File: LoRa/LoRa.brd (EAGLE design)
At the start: 59.4 x 27.9 mm, 35 parts, among them J1 UP2-AH-1-TH, U1 STM32L053C8T6, U2 RFM69HCW, U5 LM3671MF-3.3/NOPB, X1 uFL/SMA, Y1 ECS-80-S-4X

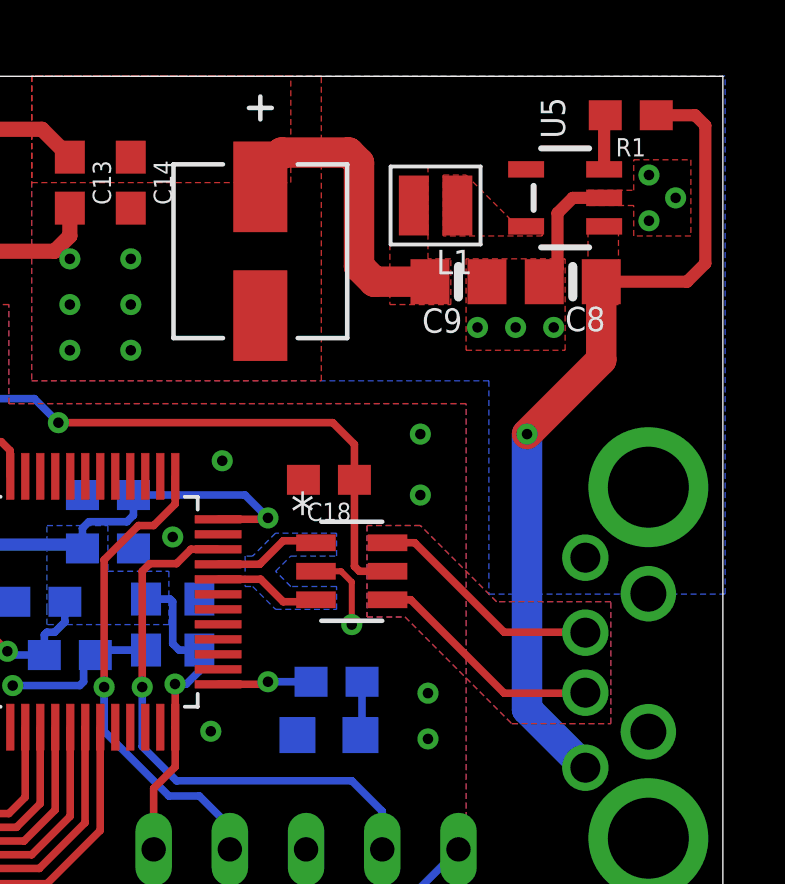
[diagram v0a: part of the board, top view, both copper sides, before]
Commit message: mounting hole and feedback trace
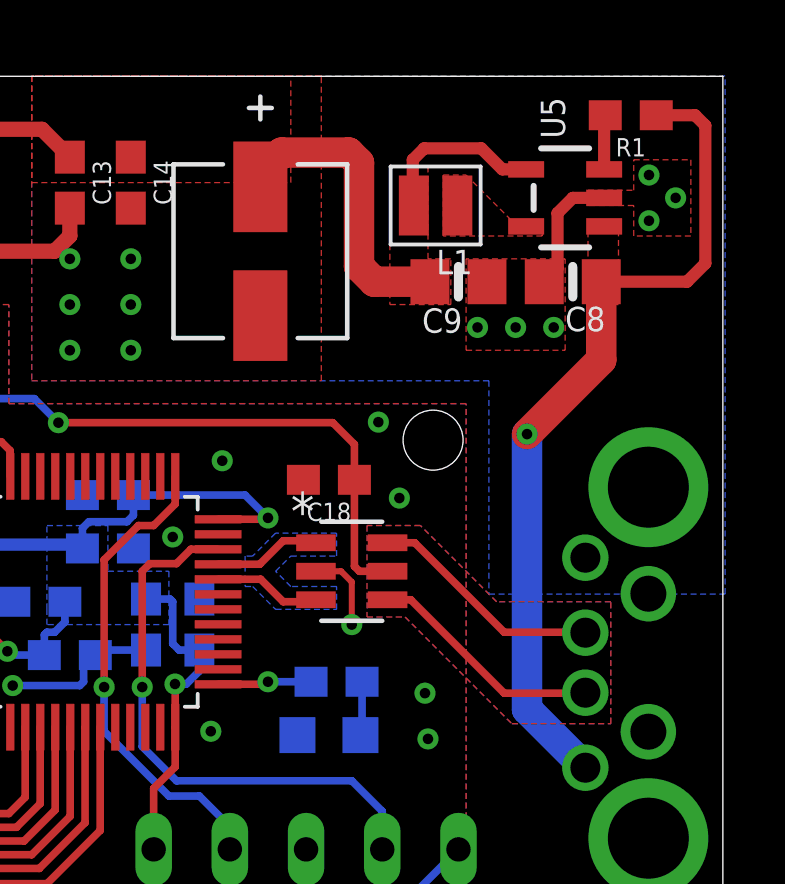
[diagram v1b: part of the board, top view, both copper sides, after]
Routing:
- net 3.3V: track 145.1 -> 150.9 mm
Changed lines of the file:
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@@
 <setting verticaltext="up"/>
 </settings>
-<grid distance="5" unitdist="mil" unit="mil" style="lines" multiple="1" display="yes" altdistance="5" altunitdist="mil" altunit="mil"/>
+<grid distance="0.1" unitdist="mm" unit="mm" style="lines" multiple="1" display="yes" altdistance="5" altunitdist="mil" altunit="mil"/>
 <layers>
 <layer number="1" name="Top" color="4" fill="1" visible="yes" active="yes"/>
@@
 <hole x="21" y="24.6" drill="2"/>
 <hole x="21" y="5.6" drill="2"/>
+<hole x="49.7" y="15.8" drill="2"/>
 </plain>
 <attributes>
@@
 <vertex x="36.322" y="27.94"/>
 </polygon>
-<via x="49.276" y="16.002" extent="1-16" drill="0.35"/>
-<via x="49.276" y="13.97" extent="1-16" drill="0.35"/>
+<via x="47.876" y="16.402" extent="1-16" drill="0.35"/>
+<via x="48.576" y="13.87" extent="1-16" drill="0.35"/>
 <wire x1="45.7962" y1="11.43" x2="46.6333375" y2="11.43" width="0.2032" layer="1"/>
 <wire x1="46.99" y1="11.0733375" x2="46.99" y2="9.652" width="0.2032" layer="1"/>
@@
 <via x="3.048" y="16.002" extent="1-16" drill="0.35"/>
 <via x="37.592" y="20.32" extent="1-16" drill="0.35"/>
-<via x="49.53" y="7.366" extent="1-16" drill="0.35"/>
+<via x="49.43" y="7.366" extent="1-16" drill="0.35"/>
 <via x="33.528" y="6.096" extent="1-16" drill="0.35"/>
 <polygon width="0.2032" layer="1" rank="4">
@@
 <wire x1="44.3103" y1="24.6126" x2="43.942" y2="24.2443" width="1.016" layer="1"/>
 <wire x1="40.386" y1="4.191" x2="40.386" y2="2.159" width="0.254" layer="1"/>
-<wire x1="49.059" y1="23.622" x2="52.8019" y2="24.826" width="0" layer="19" extent="1-1"/>
+<wire x1="52.8019" y1="24.826" x2="52.009" y2="24.826" width="0.4064" layer="1"/>
+<wire x1="49.403" y1="25.527" x2="49.022" y2="25.146" width="0.4064" layer="1"/>
+<wire x1="49.022" y1="25.146" x2="49.022" y2="23.659" width="0.4064" layer="1"/>
+<wire x1="49.022" y1="23.659" x2="49.059" y2="23.622" width="0.4064" layer="1"/>
+<wire x1="52.009" y1="24.826" x2="51.308" y2="25.527" width="0.4064" layer="1"/>
+<wire x1="51.308" y1="25.527" x2="49.403" y2="25.527" width="0.4064" layer="1"/>
 </signal>
 <signal name="RST">

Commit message: Final touches
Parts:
- removed X1: uFL/SMA, microbuilder:SMA_EDGELAUNCH_UFL
- added J4: EMPCB.SMAFSTJ.B.HT, EMPCB.SMAFSTJ.B.HT:TAOGLAS_EMPCB.SMAFSTJ.B.HT
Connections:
- net GND: now also J4.SH1, J4.SH2, J4.SH3, J4.SH4; no longer X1.GND@1, X1.GND@2, X1.GND@3, X1.GND@4
- net N$1: now also J4.1; no longer X1.P
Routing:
- net N$1: track 7.26 -> 9.14 mm
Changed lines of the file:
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@@
 <setting verticaltext="up"/>
 </settings>
-<grid distance="0.1" unitdist="mm" unit="mm" style="lines" multiple="1" display="yes" altdistance="5" altunitdist="mil" altunit="mil"/>
+<grid distance="5" unitdist="mil" unit="mil" style="lines" multiple="1" display="yes" altdistance="5" altunitdist="mil" altunit="mil"/>
 <layers>
 <layer number="1" name="Top" color="4" fill="1" visible="yes" active="yes"/>
@@
 </autorouter>
 <elements>
-<element name="J1" library="USB_Con" package="UP2-AH-1-TH" value="UP2-AH-1-TH" x="74.676" y="8.382" rot="MR270">
+<element name="J1" library="USB_Con" package="UP2-AH-1-TH" value="UP2-AH-1-TH" x="74.676" y="8.382" smashed="yes" rot="MR270">
 <attribute name="DESCRIPTION" value="USB Connectors USB 2.0 type A plug 4 pin Horizontal TH" x="74.676" y="8.382" size="1.778" layer="28" rot="MR270" display="off"/>
 <attribute name="HEIGHT" value="mm" x="74.676" y="8.382" size="1.778" layer="28" rot="MR270" display="off"/>
@@
 </element>
 <element name="U2" library="microbuilder" package="RFMHCW_SMT" value="RFM69HCW" x="9.398" y="17.78" rot="R270"/>
-<element name="X1" library="microbuilder" package="SMA_EDGELAUNCH_UFL" value="uFL/SMA" x="5.08" y="1.524" smashed="yes" rot="R90"/>
 <element name="JP2" library="microbuilder" package="1X01_ROUND" value="" x="5.08" y="6.858"/>
 <element name="C2" library="SparkFun-Capacitors" library_urn="urn:adsk.eagle:library:510" package="0603" package3d_urn="urn:adsk.eagle:package:37414/1" value="10uF" x="10.414" y="13.716" rot="MR90">
@@
 <attribute name="PROD_ID" value="RES-07856" x="46.482" y="7.747" size="1.778" layer="28" rot="MR0" display="off"/>
 </element>
+<element name="J4" library="EMPCB.SMAFSTJ.B.HT" package="TAOGLAS_EMPCB.SMAFSTJ.B.HT" value="EMPCB.SMAFSTJ.B.HT" x="5.1" y="2.7" smashed="yes">
+<attribute name="DESCRIPTION" value=" SMA Connector Jack, Female Socket 50Ohm Board Edge, End Launch Solder " x="5.1" y="2.7" size="1.778" layer="27" display="off"/>
+<attribute name="DIGI-KEY_PART_NUMBER" value="931-1175-ND" x="5.1" y="2.7" size="1.778" layer="27" display="off"/>
+<attribute name="DIGI-KEY_PURCHASE_URL" value="https://www.digikey.com/product-detail/en/taoglas-limited/EMPCB.SMAFSTJ.B.HT/931-1175-ND/3522337?utm_source=snapeda&amp;utm_medium=aggregator&amp;utm_campaign=symbol" x="5.1" y="2.7" size="1.778" layer="27" display="off"/>
+<attribute name="MF" value="Taoglas Limited" x="5.1" y="2.7" size="1.778" layer="27" display="off"/>
+<attribute name="MP" value="EMPCB.SMAFSTJ.B.HT" x="5.1" y="2.7" size="1.778" layer="27" display="off"/>
+<attribute name="NAME" x="1.786809375" y="5.9131" size="1.27121875" layer="25"/>
+<attribute name="PACKAGE" value="None" x="5.1" y="2.7" size="1.778" layer="27" display="off"/>
+</element>
 </elements>
 <signals>
@@
 <contactref element="U2" pad="2P"/>
 <contactref element="C2" pad="2"/>
-<contactref element="X1" pad="GND@2"/>
-<contactref element="X1" pad="GND@1"/>
-<contactref element="X1" pad="GND@4"/>
-<contactref element="X1" pad="GND@3"/>
 <contactref element="U1" pad="8"/>
 <contactref element="U1" pad="23"/>
@@
 <via x="42.291" y="6.096" extent="1-16" drill="0.35"/>
 <contactref element="LED1" pad="C"/>
+<contactref element="J4" pad="SH4"/>
+<contactref element="J4" pad="SH2"/>
+<contactref element="J4" pad="SH3"/>
+<contactref element="J4" pad="SH1"/>
 </signal>
 <signal name="3.3V">
@@
 </signal>
 <signal name="N$1">
-<contactref element="X1" pad="P"/>
 <contactref element="U2" pad="1P"/>
 <contactref element="JP2" pad="1"/>
-<wire x1="5.08" y1="4.572" x2="5.08" y2="6.858" width="0.4064" layer="1"/>
 <wire x1="2.398" y1="9.68" x2="2.398" y2="7.762" width="0.4064" layer="1"/>
 <wire x1="2.398" y1="7.762" x2="3.302" y2="6.858" width="0.4064" layer="1"/>
 <wire x1="3.302" y1="6.858" x2="5.08" y2="6.858" width="0.4064" layer="1"/>
+<contactref element="J4" pad="1"/>
+<wire x1="5.08" y1="6.858" x2="5.08" y2="2.72" width="0.4064" layer="1"/>
+<wire x1="5.08" y1="2.72" x2="5.1" y2="2.7" width="0.4064" layer="1"/>
 </signal>
 <signal name="USB_DP_3V3">
